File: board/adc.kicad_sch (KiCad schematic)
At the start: 11 parts, among them U1 ADS131M08, Y1 8MhZ

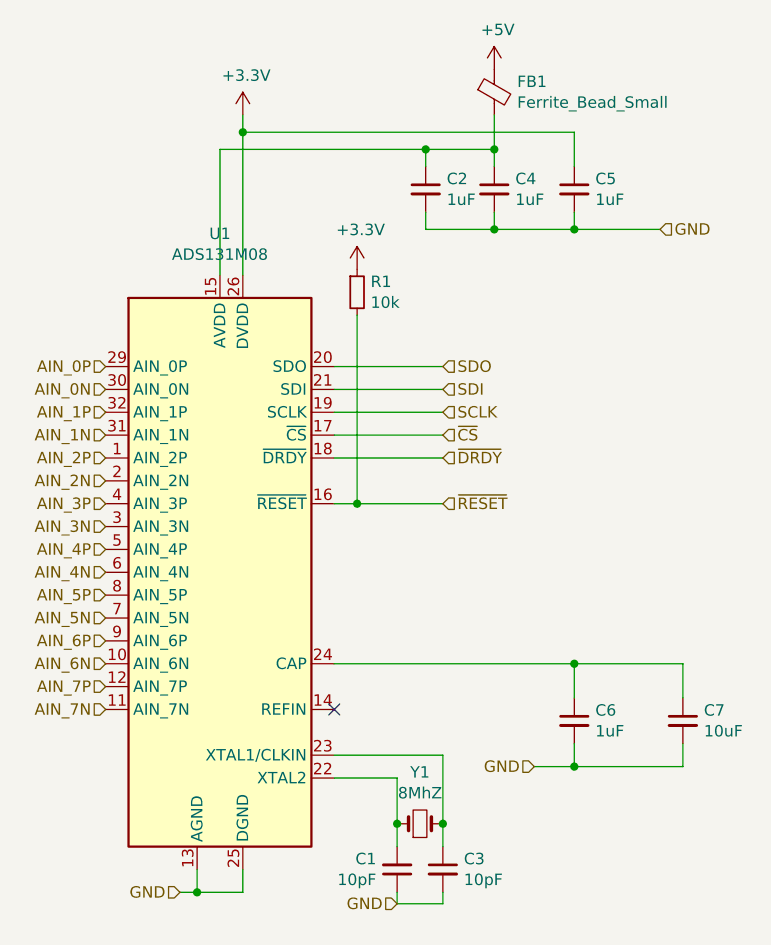
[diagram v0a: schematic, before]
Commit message: separated gnd and agnd
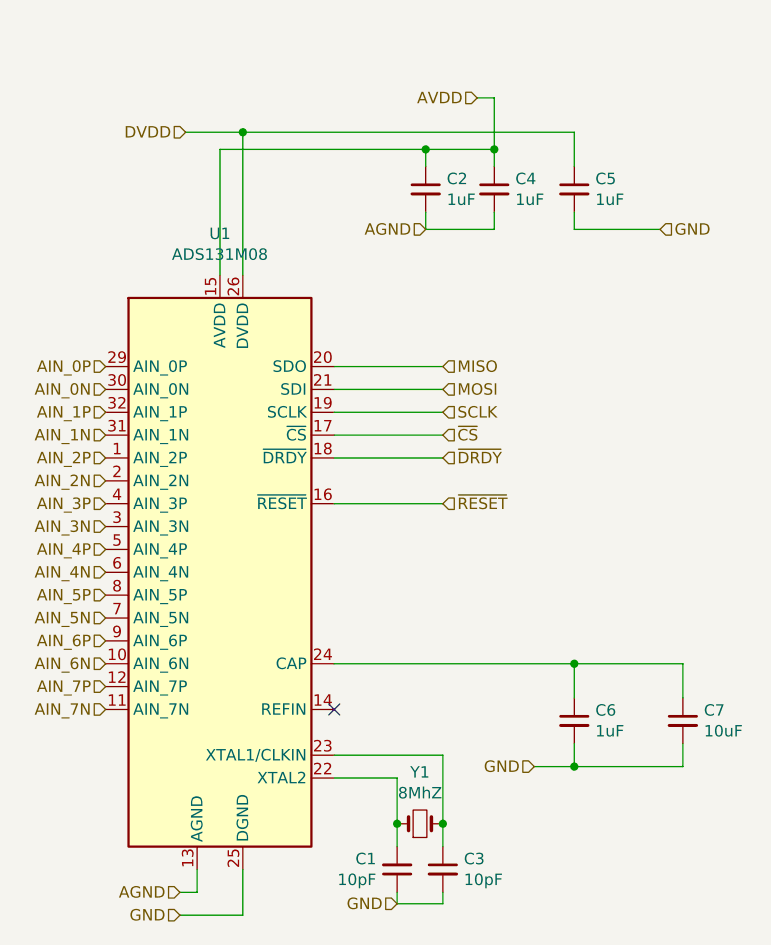
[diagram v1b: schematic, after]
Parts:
- removed FB1: Ferrite_Bead_Small, Inductor_SMD:L_0603_1608Metric, symbol Device:FerriteBead_Small
- removed R1: 10k, Resistor_SMD:R_0603_1608Metric, symbol Device:R_Small
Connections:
- net GND: no longer C2.2, C4.2, U1.13 (AGND), U1.28 (AGND), U1.33 (AGND)
- net AVDD: now reaches C2.1, C4.1, U1.15 (AVDD)
- net +3.3V renamed DVDD
- net SDI renamed MOSI
- net SDO renamed MISO
- new net AGND: C2.2, C4.2, U1.13 (AGND), U1.28 (AGND), U1.33 (AGND)
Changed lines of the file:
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@@
   (junction (at 175.895 106.045) (diameter 0) (color 0 0 0 0)
   )
-  (junction (at 167.005 57.785) (diameter 0) (color 0 0 0 0)
-  )
   (junction (at 156.21 123.825) (diameter 0) (color 0 0 0 0)
   )
-  (junction (at 175.895 57.785) (diameter 0) (color 0 0 0 0)
-  )
   (junction (at 175.895 117.475) (diameter 0) (color 0 0 0 0)
   )
   (junction (at 167.005 48.895) (diameter 0) (color 0 0 0 0)
-  )
-  (junction (at 133.985 131.445) (diameter 0) (color 0 0 0 0)
-  )
-  (junction (at 151.765 88.265) (diameter 0) (color 0 0 0 0)
   )
   (junction (at 161.29 123.825) (diameter 0) (color 0 0 0 0)
@@
     (stroke (width 0) (type default) (color 0 0 0 0))
   )
+  (wire (pts (xy 132.715 46.99) (xy 139.065 46.99))
+    (stroke (width 0) (type default) (color 0 0 0 0))
+  )
   (wire (pts (xy 175.895 55.88) (xy 175.895 57.785))
     (stroke (width 0) (type default) (color 0 0 0 0))
@@
     (stroke (width 0) (type default) (color 0 0 0 0))
   )
-  (wire (pts (xy 139.065 45.085) (xy 139.065 46.99))
-    (stroke (width 0) (type default) (color 0 0 0 0))
-  )
-  (wire (pts (xy 161.29 88.265) (xy 151.765 88.265))
-    (stroke (width 0) (type default) (color 0 0 0 0))
-  )
   (wire (pts (xy 161.29 83.185) (xy 149.225 83.185))
     (stroke (width 0) (type default) (color 0 0 0 0))
@@
     (stroke (width 0) (type default) (color 0 0 0 0))
   )
+  (wire (pts (xy 165.1 43.18) (xy 167.005 43.18))
+    (stroke (width 0) (type default) (color 0 0 0 0))
+  )
   (wire (pts (xy 161.29 123.825) (xy 161.29 126.365))
     (stroke (width 0) (type default) (color 0 0 0 0))
@@
     (stroke (width 0) (type default) (color 0 0 0 0))
   )
+  (wire (pts (xy 132.08 133.985) (xy 139.065 133.985))
+    (stroke (width 0) (type default) (color 0 0 0 0))
+  )
   (wire (pts (xy 175.895 114.935) (xy 175.895 117.475))
     (stroke (width 0) (type default) (color 0 0 0 0))
@@
     (stroke (width 0) (type default) (color 0 0 0 0))
   )
-  (wire (pts (xy 151.765 67.31) (xy 151.765 88.265))
-    (stroke (width 0) (type default) (color 0 0 0 0))
-  )
   (wire (pts (xy 161.29 75.565) (xy 149.225 75.565))
     (stroke (width 0) (type default) (color 0 0 0 0))
@@
     (stroke (width 0) (type default) (color 0 0 0 0))
   )
-  (wire (pts (xy 133.985 131.445) (xy 139.065 131.445))
-    (stroke (width 0) (type default) (color 0 0 0 0))
-  )
   (wire (pts (xy 175.895 50.8) (xy 175.895 46.99))
     (stroke (width 0) (type default) (color 0 0 0 0))
@@
     (stroke (width 0) (type default) (color 0 0 0 0))
   )
-  (wire (pts (xy 139.065 131.445) (xy 139.065 128.905))
-    (stroke (width 0) (type default) (color 0 0 0 0))
-  )
-  (wire (pts (xy 149.225 88.265) (xy 151.765 88.265))
+  (wire (pts (xy 139.065 128.905) (xy 139.065 133.985))
+    (stroke (width 0) (type default) (color 0 0 0 0))
+  )
+  (wire (pts (xy 149.225 88.265) (xy 161.29 88.265))
     (stroke (width 0) (type default) (color 0 0 0 0))
   )
@@
     (stroke (width 0) (type default) (color 0 0 0 0))
   )
-  (wire (pts (xy 167.005 57.785) (xy 175.895 57.785))
-    (stroke (width 0) (type default) (color 0 0 0 0))
-  )
-  (wire (pts (xy 167.005 45.085) (xy 167.005 48.895))
+  (wire (pts (xy 167.005 43.18) (xy 167.005 48.895))
     (stroke (width 0) (type default) (color 0 0 0 0))
   )
@@
     (stroke (width 0) (type default) (color 0 0 0 0))
   )
+  (hierarchical_label "DVDD" (shape input) (at 132.715 46.99 180)
+    (effects (font (size 1.27 1.27)) (justify right))
+  )
   (hierarchical_label "AIN_4N" (shape input) (at 123.825 95.885 180)
     (effects (font (size 1.27 1.27)) (justify right))
@@
     (effects (font (size 1.27 1.27)) (justify right))
   )
+  (hierarchical_label "GND" (shape input) (at 132.08 133.985 180)
+    (effects (font (size 1.27 1.27)) (justify right))
+  )
   (hierarchical_label "GND" (shape input) (at 171.45 117.475 180)
     (effects (font (size 1.27 1.27)) (justify right))
@@
     (effects (font (size 1.27 1.27)) (justify right))
   )
-  (hierarchical_label "SDI" (shape input) (at 161.29 75.565 0)
+  (hierarchical_label "MOSI" (shape input) (at 161.29 75.565 0)
     (effects (font (size 1.27 1.27)) (justify left))
   )
@@
     (effects (font (size 1.27 1.27)) (justify right))
   )
+  (hierarchical_label "AVDD" (shape input) (at 165.1 43.18 180)
+    (effects (font (size 1.27 1.27)) (justify right))
+  )
   (hierarchical_label "AIN_5P" (shape input) (at 123.825 98.425 180)
     (effects (font (size 1.27 1.27)) (justify right))
@@
     (effects (font (size 1.27 1.27)) (justify right))
   )
-  (hierarchical_label "SDO" (shape input) (at 161.29 73.025 0)
+  (hierarchical_label "AGND" (shape input) (at 159.385 57.785 180)
+    (effects (font (size 1.27 1.27)) (justify right))
+  )
+  (hierarchical_label "MISO" (shape input) (at 161.29 73.025 0)
     (effects (font (size 1.27 1.27)) (justify left))
   )
@@
     (effects (font (size 1.27 1.27)) (justify left))
   )
-  (hierarchical_label "GND" (shape input) (at 132.08 131.445 180)
+  (hierarchical_label "AGND" (shape input) (at 132.08 131.445 180)
     (effects (font (size 1.27 1.27)) (justify right))
   )
@@
     (pin "2")
   )
-  (symbol (lib_id "power:+5V") (at 167.005 40.005 0) (unit 1)
-    (in_bom yes) (on_board yes)
-    (property "Reference" "#PWR0105" (id 0) (at 167.005 43.815 0)
-      (effects (font (size 1.27 1.27)) hide)
-    )
-    (property "Value" "+5V" (id 1) (at 167.386 35.6108 0))
-    (property "Footprint" "" (id 2) (at 167.005 40.005 0)
-      (effects (font (size 1.27 1.27)) hide)
-    )
-    (property "Datasheet" "" (id 3) (at 167.005 40.005 0)
-      (effects (font (size 1.27 1.27)) hide)
-    )
-    (pin "1")
-  )
   (symbol (lib_id "Device:C_Small") (at 167.005 53.34 0) (unit 1)
     (in_bom yes) (on_board yes)
@@
     (pin "2")
   )
-  (symbol (lib_id "Device:FerriteBead_Small") (at 167.005 42.545 0) (unit 1)
-    (in_bom yes) (on_board yes)
-    (property "Reference" "FB1" (id 0) (at 169.545 41.3766 0)
-      (effects (font (size 1.27 1.27)) (justify left))
-    )
-    (property "Value" "Ferrite_Bead_Small" (id 1) (at 169.545 43.688 0)
-      (effects (font (size 1.27 1.27)) (justify left))
-    )
-    (property "Footprint" "Inductor_SMD:L_0603_1608Metric" (id 2) (at 165.227 42.545 90)
-      (effects (font (size 1.27 1.27)) hide)
-    )
-    (property "Datasheet" "~" (id 3) (at 167.005 42.545 0)
-      (effects (font (size 1.27 1.27)) hide)
-    )
-    (pin "1")
-    (pin "2")
-  )
-  (symbol (lib_id "power:+3.3V") (at 139.065 45.085 0) (unit 1)
-    (in_bom yes) (on_board yes)
-    (property "Reference" "#PWR0106" (id 0) (at 139.065 48.895 0)
-      (effects (font (size 1.27 1.27)) hide)
-    )
-    (property "Value" "+3.3V" (id 1) (at 139.446 40.6908 0))
-    (property "Footprint" "" (id 2) (at 139.065 45.085 0)
-      (effects (font (size 1.27 1.27)) hide)
-    )
-    (property "Datasheet" "" (id 3) (at 139.065 45.085 0)
-      (effects (font (size 1.27 1.27)) hide)
-    )
-    (pin "1")
-  )
-  (symbol (lib_id "Device:R_Small") (at 151.765 64.77 0) (unit 1)
-    (in_bom yes) (on_board yes)
-    (property "Reference" "R1" (id 0) (at 153.2636 63.6016 0)
-      (effects (font (size 1.27 1.27)) (justify left))
-    )
-    (property "Value" "10k" (id 1) (at 153.2636 65.913 0)
-      (effects (font (size 1.27 1.27)) (justify left))
-    )
-    (property "Footprint" "Resistor_SMD:R_0603_1608Metric" (id 2) (at 151.765 64.77 0)
-      (effects (font (size 1.27 1.27)) hide)
-    )
-    (property "Datasheet" "~" (id 3) (at 151.765 64.77 0)
-      (effects (font (size 1.27 1.27)) hide)
-    )
-    (pin "1")
-    (pin "2")
-  )
-  (symbol (lib_id "power:+3.3V") (at 151.765 62.23 0) (unit 1)
-    (in_bom yes) (on_board yes)
-    (property "Reference" "#PWR0102" (id 0) (at 151.765 66.04 0)
-      (effects (font (size 1.27 1.27)) hide)
-    )
-    (property "Value" "+3.3V" (id 1) (at 152.146 57.8358 0))
-    (property "Footprint" "" (id 2) (at 151.765 62.23 0)
-      (effects (font (size 1.27 1.27)) hide)
-    )
-    (property "Datasheet" "" (id 3) (at 151.765 62.23 0)
-      (effects (font (size 1.27 1.27)) hide)
-    )
-    (pin "1")
-  )
   (symbol (lib_id "Device:C_Small") (at 159.385 53.34 0) (unit 1)

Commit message: fixed footprint and added pours
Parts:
- U1: footprint Package_DFN_QFN:WQFN-32-1EP_5x5mm_P0.5mm_EP3.1x3.1mm -> Package_DFN_QFN:QFN-32-1EP_4x4mm_P0.4mm_EP2.9x2.9mm
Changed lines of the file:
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@@
     (property "Reference" "U1" (id 0) (at 136.525 58.2676 0))
     (property "Value" "ADS131M08" (id 1) (at 136.525 60.579 0))
-    (property "Footprint" "Package_DFN_QFN:WQFN-32-1EP_5x5mm_P0.5mm_EP3.1x3.1mm" (id 2) (at 136.525 95.885 0)
+    (property "Footprint" "Package_DFN_QFN:QFN-32-1EP_4x4mm_P0.4mm_EP2.9x2.9mm" (id 2) (at 136.525 95.885 0)
       (effects (font (size 1.27 1.27)) hide)
     )
